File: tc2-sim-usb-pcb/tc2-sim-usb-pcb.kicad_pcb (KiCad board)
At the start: 4 copper layers, 19.5 x 56 mm, 9 parts, among them J2 Conn_01x08

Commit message: P3-Nov release
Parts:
- added H3: MountingHole, cacophony-library:mouse-bite-10mm, F.Cu at (20.3, -7.10)
- H1, H2: footprint MountingHole:MountingHole_2.7mm_M2.5 -> cacophony-library:MountingHole_2.7mm_M2.5
- moved C2 4.71 mm to (6.70, -18.0)
- moved Card1 4.71 mm to (13.3, -14.9)
- moved USB2 0.76 mm to (16.2, 2.02)
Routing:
- net USIM_CLK: track 28.6 -> 33.7 mm
- net USIM_DATA: track 21.0 -> 26.1 mm
- net USIM_VDD: track 39.7 -> 44.6 mm
- net USIM_RST: track 25.5 -> 29.7 mm
- net GND: track 1.99 -> 5.69 mm, vias 7 -> 8
- net 4G_USB_D-: track 24.0 -> 24.7 mm
- net Net-(USB2-ID): track 3.54 -> 4.30 mm
- net Net-(USB2-VBUS): track 3.52 -> 4.28 mm
- net 4G_USB_D+: track 23.3 -> 24.1 mm
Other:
- board size 19.5 x 56 mm -> 30.3 x 58.2 mm

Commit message: v0.4.0
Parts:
- added U1: ~, cacophony-library:ziptie, F.Cu at (3.90, 25.7)
- added U2: ~, cacophony-library:ziptie, F.Cu at (3.80, 17.9)
- moved Card1 6.30 mm to (13.2, -8.60)
- moved C2 3.71 mm to (6.77, -14.3), turned to -90 degrees
- moved H3 2.82 mm to (20.3, -4.28)
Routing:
- net USIM_VDD: track 44.6 -> 37.7 mm
- net USIM_RST: track 29.7 -> 23.4 mm
- net USIM_CLK: track 33.7 -> 27.6 mm
- net USIM_DATA: track 26.1 -> 23.7 mm
- net GND: track 5.69 -> 5.36 mm, vias 8 -> 9
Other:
- outline, holes or cut-outs redrawn

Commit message: Small update for v0.4.1
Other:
- board text added: "${TAG}"
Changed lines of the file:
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@@
 		(layer "F.Fab")
+	)
+	(gr_text "${TAG}"
+		(at -1.26 -2.47 0)
+		(layer "B.SilkS")
+		(effects
+			(font
+				(size 1.5 1.5)
+				(thickness 0.3)
+				(bold yes)
+			)
+			(justify right bottom mirror)
+		)
+	)
+	(gr_text "${TAG}"
+		(at -1.35 -2.58 0)
+		(layer "F.SilkS")
+		(effects
+			(font
+				(size 1.5 1.5)
+				(thickness 0.3)
+				(bold yes)
+			)
+			(justify left bottom)
+		)
 	)
 	(segment

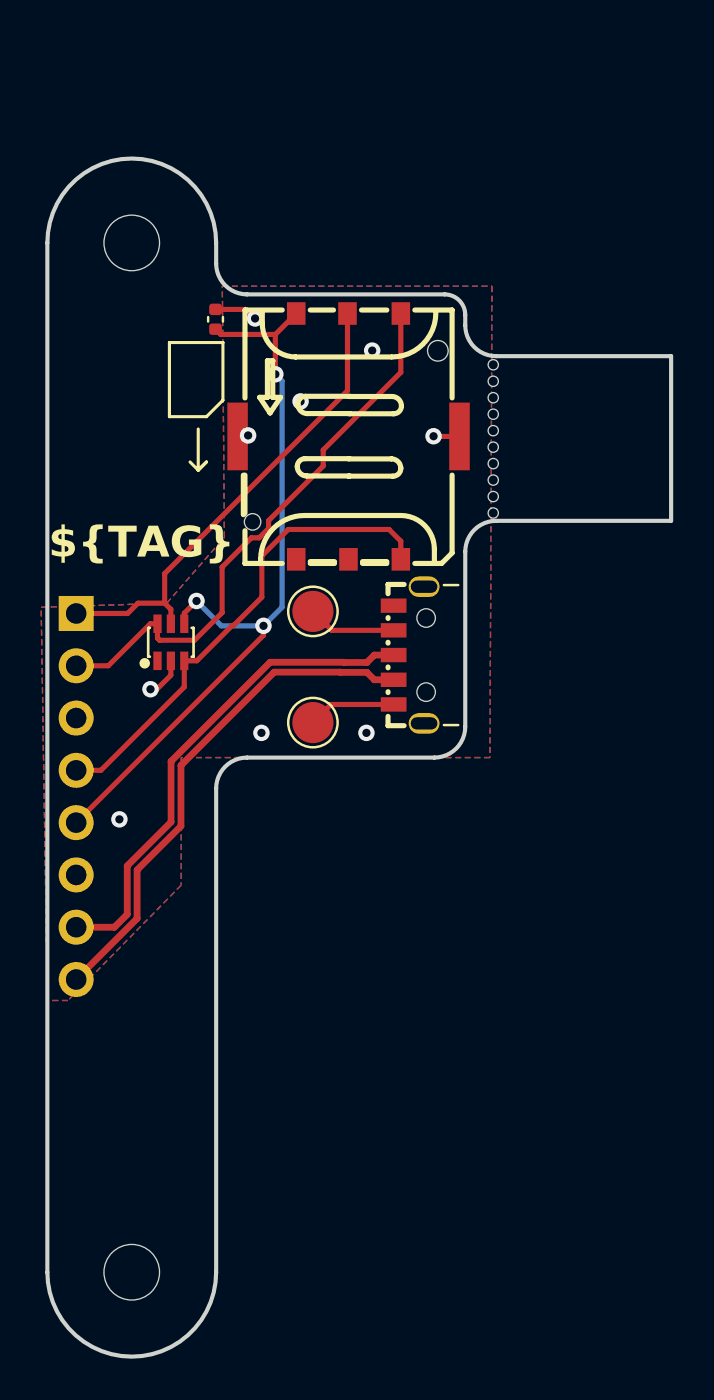
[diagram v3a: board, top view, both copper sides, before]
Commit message: Change to through hole connector and add simcard PCB to pannel
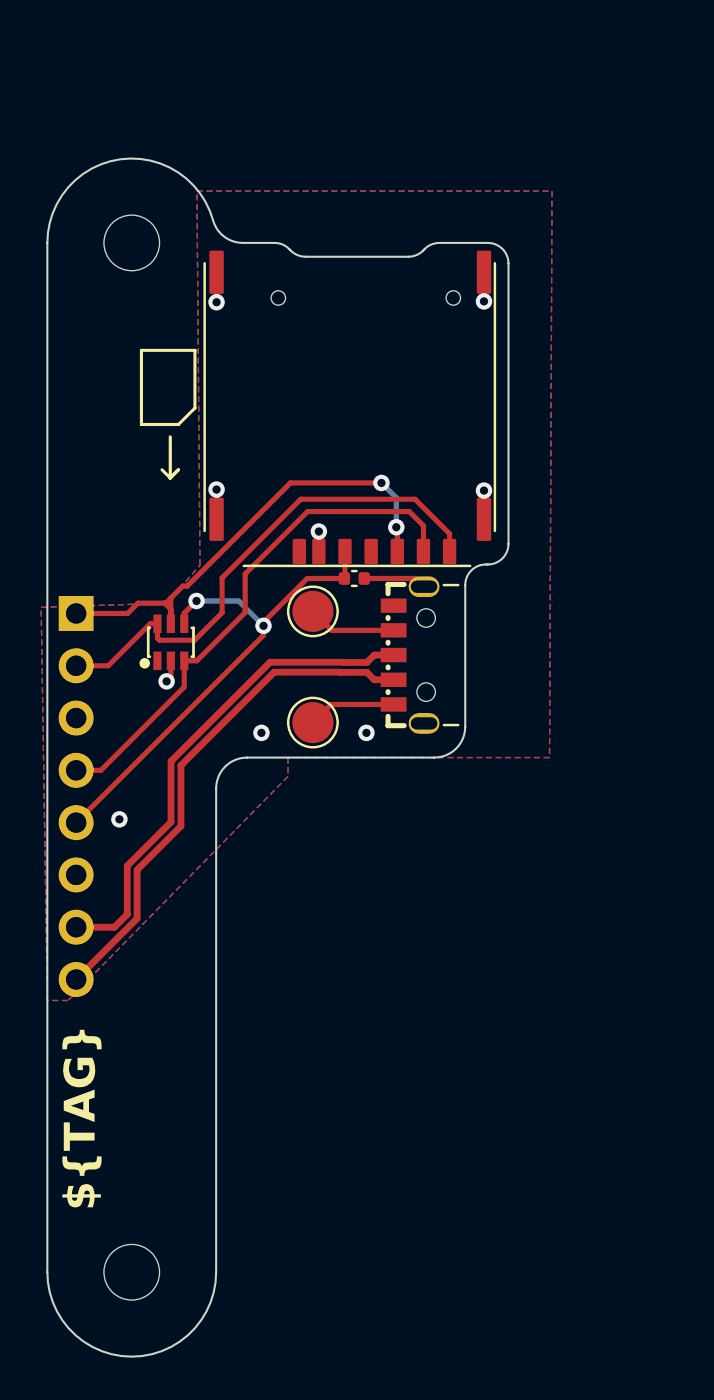
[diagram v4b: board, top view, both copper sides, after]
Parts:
- removed Card1: SIM-Nano, cacophony-library:SIM-SMD_SMN-304
- removed H3: MountingHole, cacophony-library:mouse-bite-10mm
- added REF**: Tab8mm, cacophony-library:Tab8mm, F.Cu at (21.3, -9.67)
- added REF**: Tab8mm, cacophony-library:Tab8mm, F.Cu at (6.80, 23.2)
- added REF**: Tab8mm, cacophony-library:Tab8mm, F.Cu at (-2.25, 26.5)
- added REF**: Tab8mm, cacophony-library:Tab8mm, F.Cu at (-2.11, -13.2)
- added U503: ~, cacophony-library:K-DYX-010, F.Cu at (18.1, -3.01)
- moved C501 14.3 mm to (13.5, -1.70), turned to 180 degrees
- renumbered C2 to C501, D1 to D501, H1 to H501, H2 to H502, J2 to J501, TP1 to TP501, TP2 to TP502, U1 to U501, U2 to U502, USB2 to USB501
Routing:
- net USIM_VDD: track 37.7 -> 24.9 mm, vias 3 -> 2
- net GND: track 5.36 -> 10.5 mm
- net USIM_CLK: track 27.6 -> 25.1 mm
- net USIM_DATA: track 23.7 -> 25.5 mm
- net USIM_RST: track 23.4 -> 23.8 mm, vias 0 -> 2
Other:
- board size 30.3 x 58.2 mm -> 22.4 x 58.2 mm

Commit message: Version v0.7.0
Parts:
- removed TP501, TP502: TestPoint, TestPoint:TestPoint_Pad_D2.0mm
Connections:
- USB501 pad 1: Net-(USB501-VBUS) -> unconnected-(USB501-VBUS-Pad1)
- USB501 pad 4: Net-(USB501-ID) -> unconnected-(USB501-ID-Pad4)
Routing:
- net Net-(USB501-ID): track 4.30 -> 0.00 mm
- net Net-(USB501-VBUS): track 4.28 -> 0.00 mm
- added copper zone on In4.Cu, net GND
- removed copper zone on In2.Cu, net GND
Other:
- copper layers 4 -> 6

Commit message: v0.7.2 panelise microphone boards
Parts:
- REF** (x4): value Tab8mm -> Tab; footprint cacophony-library:Tab8mm -> PCM_kikit:Tab
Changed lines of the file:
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@@
 		)
 	)
-	(footprint "cacophony-library:Tab8mm"
+	(footprint "PCM_kikit:Tab"
 		(layer "F.Cu")
 		(at 21.28 -9.67 180)
 		(descr "A symbol representing annotation for tab placement")
 		(property "Reference" "REF**"
-			(at -0.25 -2 0)
-			(layer "F.SilkS")
-			(hide yes)
-			(effects
-				(font
-					(size 1 1)
-					(thickness 0.15)
-				)
-			)
-		)
-		(property "Value" "Tab8mm"
-			(at -3 -1 0)
+			(at -0.25 -2 180)
+			(layer "F.SilkS")
+			(hide yes)
+			(effects
+				(font
+					(size 1 1)
+					(thickness 0.15)
+				)
+			)
+		)
+		(property "Value" "Tab"
+			(at -3 -1 180)
 			(layer "Dwgs.User")
 			(effects
@@
 			)
 		)
-		(property "Footprint" "cacophony-library:Tab8mm"
+		(property "Footprint" "PCM_kikit:Tab"
 			(at 0 0 180)
-			(unlocked yes)
 			(layer "F.Fab")
 			(hide yes)
@@
 		(property "Datasheet" ""
 			(at 0 0 180)
-			(unlocked yes)
 			(layer "F.Fab")
 			(hide yes)
@@
 		(property "Description" ""
 			(at 0 0 180)
-			(unlocked yes)
-			(layer "F.Fab")
-			(hide yes)
-			(effects
-				(font
-					(size 1.27 1.27)
-					(thickness 0.15)
-				)
-			)
-		)
-		(attr board_only exclude_from_pos_files exclude_from_bom allow_missing_courtyard
-			dnp
-		)
+			(layer "F.Fab")
+			(hide yes)
+			(effects
+				(font
+					(size 1.27 1.27)
+					(thickness 0.15)
+				)
+			)
+		)
+		(attr board_only exclude_from_pos_files exclude_from_bom allow_missing_courtyard)
 		(fp_line
 			(start 0 1)
@@
 		)
 	)
-	(footprint "cacophony-library:Tab8mm"
+	(footprint "PCM_kikit:Tab"
 		(layer "F.Cu")
 		(at 6.8 23.211 180)
 		(descr "A symbol representing annotation for tab placement")
 		(property "Reference" "REF**"
-			(at -0.25 -2 0)
-			(layer "F.SilkS")
-			(hide yes)
-			(effects
-				(font
-					(size 1 1)
-					(thickness 0.15)
-				)
-			)
-		)
-		(property "Value" "Tab8mm"
-			(at -3 -1 0)
+			(at -0.25 -2 180)
+			(layer "F.SilkS")
+			(hide yes)
+			(effects
+				(font
+					(size 1 1)
+					(thickness 0.15)
+				)
+			)
+		)
+		(property "Value" "Tab"
+			(at -3 -1 180)
 			(layer "Dwgs.User")
 			(effects
@@
 			)
 		)
-		(property "Footprint" "cacophony-library:Tab8mm"
+		(property "Footprint" "PCM_kikit:Tab"
 			(at 0 0 180)
-			(unlocked yes)
 			(layer "F.Fab")
 			(hide yes)
@@
 		(property "Datasheet" ""
 			(at 0 0 180)
-			(unlocked yes)
 			(layer "F.Fab")
 			(hide yes)
@@
 		(property "Description" ""
 			(at 0 0 180)
-			(unlocked yes)
-			(layer "F.Fab")
-			(hide yes)
-			(effects
-				(font
-					(size 1.27 1.27)
-					(thickness 0.15)
-				)
-			)
-		)
-		(attr board_only exclude_from_pos_files exclude_from_bom allow_missing_courtyard
-			dnp
-		)
+			(layer "F.Fab")
+			(hide yes)
+			(effects
+				(font
+					(size 1.27 1.27)
+					(thickness 0.15)
+				)
+			)
+		)
+		(attr board_only exclude_from_pos_files exclude_from_bom allow_missing_courtyard)
 		(fp_line
 			(start 0 1)
@@
 		)
 	)
-	(footprint "cacophony-library:Tab8mm"
+	(footprint "PCM_kikit:Tab"
 		(layer "F.Cu")
 		(at -2.25 26.5)
@@
 			)
 		)
-		(property "Value" "Tab8mm"
+		(property "Value" "Tab"
 			(at -3 -1 0)
 			(layer "Dwgs.User")
@@
 			)
 		)
-		(property "Footprint" "cacophony-library:Tab8mm"
-			(at 0 0 0)
-			(unlocked yes)
+		(property "Footprint" "PCM_kikit:Tab"
+			(at 0 0 0)
 			(layer "F.Fab")
 			(hide yes)
@@
 		(property "Datasheet" ""
 			(at 0 0 0)
-			(unlocked yes)
 			(layer "F.Fab")
 			(hide yes)
@@
 		(property "Description" ""
 			(at 0 0 0)
-			(unlocked yes)
-			(layer "F.Fab")
-			(hide yes)
-			(effects
-				(font
-					(size 1.27 1.27)
-					(thickness 0.15)
-				)
-			)
-		)
-		(attr board_only exclude_from_pos_files exclude_from_bom allow_missing_courtyard
-			dnp
-		)
+			(layer "F.Fab")
+			(hide yes)
+			(effects
+				(font
+					(size 1.27 1.27)
+					(thickness 0.15)
+				)
+			)
+		)
+		(attr board_only exclude_from_pos_files exclude_from_bom allow_missing_courtyard)
 		(fp_line
 			(start 0 0)
@@
 		)
 	)
-	(footprint "cacophony-library:Tab8mm"
+	(footprint "PCM_kikit:Tab"
 		(layer "F.Cu")
 		(at -2.11 -13.25)
@@
 			)
 		)
-		(property "Value" "Tab8mm"
+		(property "Value" "Tab"
 			(at -3 -1 0)
 			(layer "Dwgs.User")
@@
 			)
 		)
-		(property "Footprint" "cacophony-library:Tab8mm"
-			(at 0 0 0)
-			(unlocked yes)
+		(property "Footprint" "PCM_kikit:Tab"
+			(at 0 0 0)
 			(layer "F.Fab")
 			(hide yes)
@@
 		(property "Datasheet" ""
 			(at 0 0 0)
-			(unlocked yes)
 			(layer "F.Fab")
 			(hide yes)
@@
 		(property "Description" ""
 			(at 0 0 0)
-			(unlocked yes)
-			(layer "F.Fab")
-			(hide yes)
-			(effects
-				(font
-					(size 1.27 1.27)
-					(thickness 0.15)
-				)
-			)
-		)
-		(attr board_only exclude_from_pos_files exclude_from_bom allow_missing_courtyard
-			dnp
-		)
+			(layer "F.Fab")
+			(hide yes)
+			(effects
+				(font
+					(size 1.27 1.27)
+					(thickness 0.15)
+				)
+			)
+		)
+		(attr board_only exclude_from_pos_files exclude_from_bom allow_missing_courtyard)
 		(fp_line
 			(start 0 0)

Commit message: v0.7.3
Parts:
- moved REF** 4.55 mm to (-2.25, 21.9)
- moved REF** 2.38 mm to (-2.11, -10.9)
- moved REF** 1.00 mm to (21.0, -10.6)
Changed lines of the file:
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@@
-		)
-	)
-	(footprint "PCM_kikit:Tab"
-		(layer "F.Cu")
-		(at 21.28 -9.67 180)
-		(descr "A symbol representing annotation for tab placement")
-		(property "Reference" "REF**"
-			(at -0.25 -2 180)
-			(layer "F.SilkS")
-			(hide yes)
-			(effects
-				(font
-					(size 1 1)
-					(thickness 0.15)
-				)
-			)
-		)
-		(property "Value" "Tab"
-			(at -3 -1 180)
-			(layer "Dwgs.User")
-			(effects
-				(font
-					(size 1.2 1.2)
-					(thickness 0.2)
-				)
-			)
-		)
-		(property "Footprint" "PCM_kikit:Tab"
-			(at 0 0 180)
-			(layer "F.Fab")
-			(hide yes)
-			(effects
-				(font
-					(size 1.27 1.27)
-					(thickness 0.15)
-				)
-			)
-		)
-		(property "Datasheet" ""
-			(at 0 0 180)
-			(layer "F.Fab")
-			(hide yes)
-			(effects
-				(font
-					(size 1.27 1.27)
-					(thickness 0.15)
-				)
-			)
-		)
-		(property "Description" ""
-			(at 0 0 180)
-			(layer "F.Fab")
-			(hide yes)
-			(effects
-				(font
-					(size 1.27 1.27)
-					(thickness 0.15)
-				)
-			)
-		)
-		(attr board_only exclude_from_pos_files exclude_from_bom allow_missing_courtyard)
-		(fp_line
-			(start 0 1)
-			(end 0 -1)
-			(stroke
-				(width 0.3)
-				(type solid)
-			)
-			(layer "Dwgs.User")
-		)
-		(fp_line
-			(start 0 0)
-			(end -1 1)
-			(stroke
-				(width 0.3)
-				(type solid)
-			)
-			(layer "Dwgs.User")
-		)
-		(fp_line
-			(start 0 0)
-			(end -1 -1)
-			(stroke
-				(width 0.3)
-				(type solid)
-			)
-			(layer "Dwgs.User")
-		)
-		(fp_line
-			(start 0 0)
-			(end -3 0)
-			(stroke
-				(width 0.3)
-				(type solid)
-			)
-			(layer "Dwgs.User")
-		)
-		(fp_text user "KIKIT: width: 8mm"
-			(at -5.5 0 90)
-			(layer "Dwgs.User")
-			(effects
-				(font
-					(size 1 1)
-					(thickness 0.15)
-				)
-			)
 		)
 	)
@@
 			(rotate
 				(xyz 0 0 180)
+			)
+		)
+	)
+	(footprint "PCM_kikit:Tab"
+		(layer "F.Cu")
+		(at 21 -10.63 180)
+		(descr "A symbol representing annotation for tab placement")
+		(property "Reference" "REF**"
+			(at -0.25 -2 180)
+			(layer "F.SilkS")
+			(hide yes)
+			(effects
+				(font
+					(size 1 1)
+					(thickness 0.15)
+				)
+			)
+		)
+		(property "Value" "Tab"
+			(at -3 -1 180)
+			(layer "Dwgs.User")
+			(effects
+				(font
+					(size 1.2 1.2)
+					(thickness 0.2)
+				)
+			)
+		)
+		(property "Footprint" "PCM_kikit:Tab"
+			(at 0 0 180)
+			(layer "F.Fab")
+			(hide yes)
+			(effects
+				(font
+					(size 1.27 1.27)
+					(thickness 0.15)
+				)
+			)
+		)
+		(property "Datasheet" ""
+			(at 0 0 180)
+			(layer "F.Fab")
+			(hide yes)
+			(effects
+				(font
+					(size 1.27 1.27)
+					(thickness 0.15)
+				)
+			)
+		)
+		(property "Description" ""
+			(at 0 0 180)
+			(layer "F.Fab")
+			(hide yes)
+			(effects
+				(font
+					(size 1.27 1.27)
+					(thickness 0.15)
+				)
+			)
+		)
+		(attr board_only exclude_from_pos_files exclude_from_bom allow_missing_courtyard)
+		(fp_line
+			(start 0 1)
+			(end 0 -1)
+			(stroke
+				(width 0.3)
+				(type solid)
+			)
+			(layer "Dwgs.User")
+		)
+		(fp_line
+			(start 0 0)
+			(end -1 1)
+			(stroke
+				(width 0.3)
+				(type solid)
+			)
+			(layer "Dwgs.User")
+		)
+		(fp_line
+			(start 0 0)
+			(end -1 -1)
+			(stroke
+				(width 0.3)
+				(type solid)
+			)
+			(layer "Dwgs.User")
+		)
+		(fp_line
+			(start 0 0)
+			(end -3 0)
+			(stroke
+				(width 0.3)
+				(type solid)
+			)
+			(layer "Dwgs.User")
+		)
+		(fp_text user "KIKIT: width: 8mm"
+			(at -5.5 0 90)
+			(layer "Dwgs.User")
+			(effects
+				(font
+					(size 1 1)
+					(thickness 0.15)
+				)
 			)
 		)
@@
 	(footprint "PCM_kikit:Tab"
 		(layer "F.Cu")
-		(at -2.25 26.5)
+		(at -2.25 21.95)
 		(descr "A symbol representing annotation for tab placement")
 		(property "Reference" "REF**"
@@
 	(footprint "PCM_kikit:Tab"
 		(layer "F.Cu")
-		(at -2.11 -13.25)
+		(at -2.11 -10.87)
 		(descr "A symbol representing annotation for tab placement")
 		(property "Reference" "REF**"
@@
 			)
 		)
+		(property "LCSC" "C5156616"
+			(at 0 0 180)
+			(unlocked yes)
+			(layer "B.Fab")
+			(hide yes)
+			(effects
+				(font
+					(size 1 1)
+					(thickness 0.15)
+				)
+				(justify mirror)
+			)
+		)
 		(property ki_fp_filters "Connector*:*_1x??_*")
 		(sheetname "Root")
 		(sheetfile "tc2-sim-usb-pcb.kicad_sch")
-		(attr through_hole exclude_from_bom)
+		(attr through_hole exclude_from_bom dnp)
 		(fp_line
 			(start 1.33 -1.27)

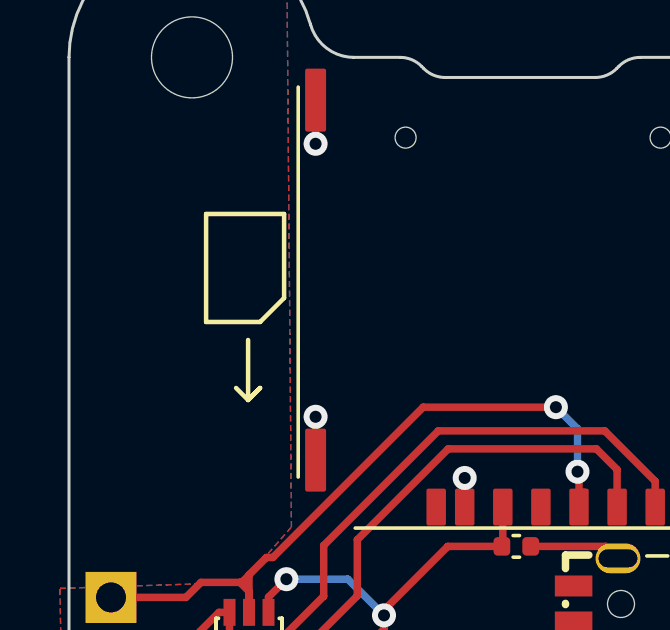
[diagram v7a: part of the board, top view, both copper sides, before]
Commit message: Updated to use field LCSC Part instead of LCSC for the JLCPCB part number
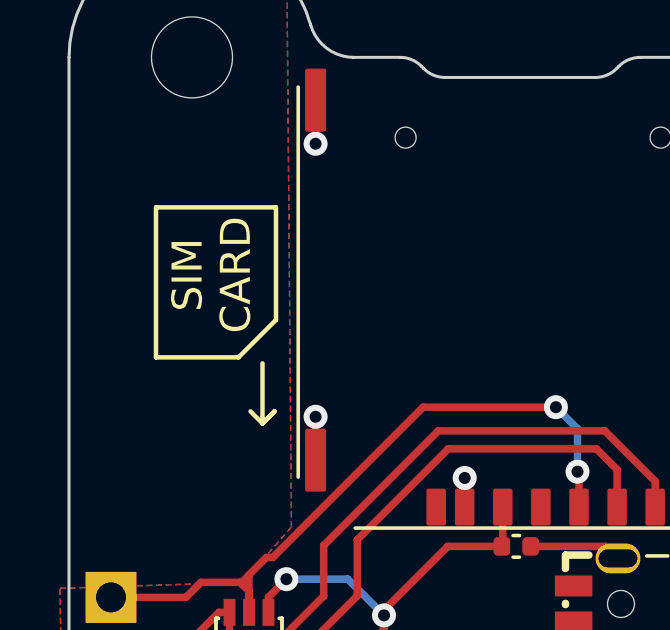
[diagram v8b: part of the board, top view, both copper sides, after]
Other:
- board text added: "SIM CARD"
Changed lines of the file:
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@@
 			)
 		)
-		(property "LCSC" "C16772"
+		(property "LCSC Part" "C16772"
 			(at 0 0 90)
 			(layer "F.Fab")
@@
 			)
 		)
-		(property "LCSC" "C15879"
+		(property "LCSC Part" "C15879"
 			(at 0 0 0)
 			(layer "F.Fab")
@@
 			)
 		)
-		(property "LCSC" "C2919617"
+		(property "LCSC Part" "C2919617"
 			(at 15.91 -12.68 90)
 			(unlocked yes)
@@
 			)
 		)
-		(property "LCSC" "C5156616"
+		(property "LCSC Part" "C5156616"
 			(at 0 0 180)
 			(unlocked yes)
@@
 	)
 	(gr_line
-		(start 4.57 -6.58)
-		(end 4.97 -6.98)
+		(start 5.05 -5.8)
+		(end 5.45 -6.2)
 		(stroke
 			(width 0.15)
@@
 	)
 	(gr_line
-		(start 4.17 -6.98)
-		(end 4.57 -6.58)
+		(start 4.65 -6.2)
+		(end 5.05 -5.8)
 		(stroke
 			(width 0.15)
@@
 	)
 	(gr_line
-		(start 4.97 -6.98)
-		(end 4.57 -6.58)
+		(start 5.45 -6.2)
+		(end 5.05 -5.8)
 		(stroke
 			(width 0.15)
@@
 	)
 	(gr_line
-		(start 3.17 -12.78)
-		(end 5.77 -12.78)
+		(start 1.5 -13)
+		(end 5.5 -13)
 		(stroke
 			(width 0.15)
@@
 	)
 	(gr_line
-		(start 3.17 -9.18)
-		(end 3.17 -12.78)
+		(start 1.5 -8)
+		(end 1.5 -13)
 		(stroke
 			(width 0.15)
@@
 	)
 	(gr_line
-		(start 4.97 -9.18)
-		(end 3.17 -9.18)
+		(start 4.25 -8)
+		(end 1.5 -8)
 		(stroke
 			(width 0.15)
@@
 	)
 	(gr_line
-		(start 5.77 -12.78)
-		(end 5.77 -9.98)
+		(start 5.5 -13)
+		(end 5.5 -9.25)
 		(stroke
 			(width 0.15)
@@
 	)
 	(gr_line
-		(start 5.77 -9.98)
-		(end 4.97 -9.18)
+		(start 5.5 -9.25)
+		(end 4.25 -8)
 		(stroke
 			(width 0.15)
@@
 	)
 	(gr_line
-		(start 4.57 -8.58)
-		(end 4.57 -6.58)
+		(start 5.05 -7.8)
+		(end 5.05 -5.8)
 		(stroke
 			(width 0.15)
@@
 		)
 	)
+	(gr_text "SIM\nCARD"
+		(at 4.75 -10.75 90)
+		(layer "F.SilkS")
+		(effects
+			(font
+				(size 1 1)
+				(thickness 0.15)
+			)
+			(justify bottom)
+		)
+	)
 	(segment
 		(start 0 7.62)
@@
 		(members "0a801779-da41-41ab-8056-84bb15e2ae81" "5b462ebf-75a6-472e-9994-d76513cea6d7"
 			"5d942e5a-b690-4ffc-905b-39ec0af5f9e1" "9d860655-92e1-4a93-a140-d3bad75f517b"
-			"bb0952dd-33d3-4e40-97c3-edbc6c9091cd" "c05d5d90-b3e0-4cb4-9974-727b0a49559f"
-			"d7b375f0-4d7a-4a5f-bfb4-f1abe1507d43" "f64659a7-c5cf-487c-a73b-8a40952dbb4c"
-			"fad5446a-78e7-4b13-a7b9-a10f7eb02ac4"
+			"a2adfc46-70d2-493c-8991-8fc4f632c1ea" "bb0952dd-33d3-4e40-97c3-edbc6c9091cd"
+			"c05d5d90-b3e0-4cb4-9974-727b0a49559f" "d7b375f0-4d7a-4a5f-bfb4-f1abe1507d43"
+			"f64659a7-c5cf-487c-a73b-8a40952dbb4c" "fad5446a-78e7-4b13-a7b9-a10f7eb02ac4"
 		)
 	)
 	(group ""
-		(members "918be66b-bd09-4fc3-8597-1c1f1fb27908")
-	)
-	(group ""
